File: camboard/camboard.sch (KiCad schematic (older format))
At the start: 36 parts

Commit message: Fixed camera connections
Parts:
- removed U?: STM32F746VGT6, symbol STM32F746VGT6
- added U?: STM32F746VGT6, symbol STM32F746VGT6
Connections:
- net labels added: DCMI_D0, DCMI_D1, DCMI_D2, DCMI_D3, DCMI_D4, DCMI_D5, DCMI_D6, DCMI_D7, DCMI_PWDN, WKUP
- wire segments 61 -> 82
- no-connect marks 7 -> 10
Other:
- moved on the sheet: J?
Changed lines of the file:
@@
 L PPTC102LFBN-RC J?
 U 1 1 59CC1D8B
-P 3200 2350
-F 0 "J?" H 3350 2850 50  0000 C CNN
-F 1 "PPTC102LFBN-RC" H 3400 1750 50  0000 C CNN
-F 2 "Pin_Headers:Pin_Header_Straight_2x10_Pitch2.54mm" H 1850 2200 50  0001 C CNN
-F 3 "" H 3500 2850 50  0001 C CNN
-	1    3200 2350
+P 4350 2400
+F 0 "J?" H 4500 2900 50  0000 C CNN
+F 1 "PPTC102LFBN-RC" H 4550 1800 50  0000 C CNN
+F 2 "Pin_Headers:Pin_Header_Straight_2x10_Pitch2.54mm" H 3000 2250 50  0001 C CNN
+F 3 "" H 4650 2900 50  0001 C CNN
+	1    4350 2400
 	1    0    0    -1
 $EndComp
 Text Label 8200 5325 1    60   ~ 0
 OSC25M
-Text Label 4000 2250 0    60   ~ 0
+Text Label 4150 2500 2    60   ~ 0
 OSC25M
-$Comp
-L STM32F746VGT6 U?
-U 1 1 59CAFAA7
-P 1125 2050
-F 0 "U?" H 1325 2300 60  0000 L CNN
-F 1 "STM32F746VGT6" H 1325 2200 60  0000 L CNN
-F 2 "" H 1125 2050 60  0001 C CNN
-F 3 "" H 1125 2050 60  0001 C CNN
-	1    1125 2050
-	1    0    0    -1
-$EndComp
-NoConn ~ 3000 2050
-NoConn ~ 3750 2050
 $Comp
 L +3V3 #PWR?
 U 1 1 59CC45D1
-P 3000 1950
-F 0 "#PWR?" H 3000 1800 50  0001 C CNN
-F 1 "+3V3" H 3000 2090 50  0000 C CNN
-F 2 "" H 3000 1950 50  0001 C CNN
-F 3 "" H 3000 1950 50  0001 C CNN
-	1    3000 1950
+P 4150 2000
+F 0 "#PWR?" H 4150 1850 50  0001 C CNN
+F 1 "+3V3" H 4150 2140 50  0000 C CNN
+F 2 "" H 4150 2000 50  0001 C CNN
+F 3 "" H 4150 2000 50  0001 C CNN
+	1    4150 2000
 	1    0    0    -1
 $EndComp
@@
 L GND #PWR?
 U 1 1 59CC4735
-P 3900 1950
-F 0 "#PWR?" H 3900 1700 50  0001 C CNN
-F 1 "GND" H 3900 1800 50  0000 C CNN
-F 2 "" H 3900 1950 50  0001 C CNN
-F 3 "" H 3900 1950 50  0001 C CNN
-	1    3900 1950
+P 4150 2900
+F 0 "#PWR?" H 4150 2650 50  0001 C CNN
+F 1 "GND" H 4150 2750 50  0000 C CNN
+F 2 "" H 4150 2900 50  0001 C CNN
+F 3 "" H 4150 2900 50  0001 C CNN
+	1    4150 2900
 	1    0    0    -1
 $EndComp
@@
 Text Label 1850 5975 0    60   ~ 0
 USB_5V
-Wire Wire Line
-	7700 5375 7375 5375
-Wire Wire Line
-	7375 5375 7375 5825
-Wire Wire Line
-	7675 5825 7700 5825
-Wire Wire Line
-	7700 5825 7700 5675
-Wire Wire Line
-	10000 5525 10450 5525
-Wire Wire Line
-	10000 5825 10450 5825
-Connection ~ 10225 5525
-Connection ~ 10225 5825
-Wire Wire Line
-	9700 5625 9700 5825
-Wire Wire Line
-	3550 6175 5225 6175
-Wire Wire Line
-	5225 6175 5225 6475
-Wire Wire Line
-	5225 6475 5150 6475
-Wire Wire Line
-	5150 6375 5150 6250
-Wire Wire Line
-	5150 6250 3550 6250
-Wire Wire Line
-	3550 6250 3550 6275
-Wire Wire Line
-	2825 4250 3625 4250
-Wire Wire Line
-	2900 4250 2900 3875
-Wire Wire Line
-	2825 4350 3625 4350
-Wire Wire Line
-	3050 4350 3050 3875
-Wire Wire Line
-	2825 4450 3625 4450
-Wire Wire Line
-	3200 4450 3200 3875
-Wire Wire Line
-	2825 4550 3625 4550
-Wire Wire Line
-	3350 4550 3350 3875
-Wire Wire Line
-	2825 4650 3625 4650
-Wire Wire Line
-	3500 4650 3500 3875
-Wire Wire Line
-	2825 4150 3625 4150
-Connection ~ 2900 4250
-Connection ~ 3050 4350
-Connection ~ 3200 4450
-Connection ~ 3350 4550
-Connection ~ 3500 4650
-Wire Wire Line
-	2900 3575 3500 3575
-Connection ~ 3050 3575
-Connection ~ 3200 3575
-Connection ~ 3350 3575
-Wire Wire Line
-	2725 2550 2850 2550
-Wire Wire Line
-	2850 2550 2850 2250
-Wire Wire Line
-	2850 2250 3000 2250
-Wire Wire Line
-	8200 5525 8200 5325
-Wire Wire Line
-	3000 2850 2725 2850
-Wire Wire Line
-	2725 2850 2725 2650
-Wire Wire Line
-	2725 2450 2800 2450
-Wire Wire Line
-	2800 2450 2800 3025
-Wire Wire Line
-	2800 3025 3750 3025
-Wire Wire Line
-	3750 3025 3750 2850
-Wire Wire Line
-	3750 1950 3900 1950
-Wire Wire Line
-	4000 2250 3750 2250
-Wire Wire Line
-	6275 1000 6375 1000
-Connection ~ 6325 1000
-Wire Wire Line
-	6975 1300 7450 1300
-Wire Wire Line
-	7450 1300 7450 1600
-Wire Wire Line
-	6975 1700 7450 1700
-Wire Wire Line
-	6975 1800 7450 1800
-Wire Wire Line
-	6975 1900 7450 1900
-Wire Wire Line
-	6975 2000 7450 2000
-Wire Wire Line
-	6975 2300 7025 2300
-Wire Wire Line
-	7025 2300 7025 2375
-Wire Wire Line
-	6975 2200 7200 2200
-Wire Wire Line
-	7200 2200 7200 2375
-Wire Wire Line
-	6975 1600 7375 1600
-Wire Wire Line
-	7375 1600 7375 2375
-Wire Wire Line
-	2075 7275 2950 7275
-Connection ~ 2850 7275
-Wire Wire Line
-	1975 6825 2075 6825
-Wire Wire Line
-	2075 6675 2075 6975
-Wire Wire Line
-	2075 6675 2150 6675
-Wire Wire Line
-	2150 6775 2075 6775
-Connection ~ 2075 6775
-Wire Wire Line
-	2075 6875 2150 6875
-Connection ~ 2075 6825
-Wire Wire Line
-	2075 6975 2150 6975
-Connection ~ 2075 6875
 $Comp
 L GND #PWR?
@@
 	1    0    0    -1
 $EndComp
-Connection ~ 2750 7275
 $Comp
 L LED D?
@@
 	1    0    0    -1
 $EndComp
-Wire Wire Line
-	5550 6650 5550 6775
-Wire Wire Line
-	5550 6775 3550 6775
-Wire Wire Line
-	5875 6650 5875 6875
-Wire Wire Line
-	5875 6875 3550 6875
 Text Notes 8825 6350 0    60   ~ 0
 Oscillators
@@
 Text Notes 2850 5325 0    60   ~ 0
 uSD Card
-Text Notes 2400 3250 0    60   ~ 0
+Text Notes 2250 3050 0    60   ~ 0
 Camera DCMI
 Text Notes 6450 3075 0    60   ~ 0
@@
 Text Notes 1900 1575 0    60   ~ 0
 Power
+$Comp
+L STM32F746VGT6 U?
+U 1 1 59CD63AE
+P 1650 2000
+F 0 "U?" H 1850 2250 60  0000 L CNN
+F 1 "STM32F746VGT6" H 1850 2150 60  0000 L CNN
+F 2 "" H 1650 2000 60  0001 C CNN
+F 3 "" H 1650 2000 60  0001 C CNN
+	1    1650 2000
+	1    0    0    -1
+$EndComp
+NoConn ~ 3350 2300
+NoConn ~ 3350 2400
+Text Label 1650 2000 2    60   ~ 0
+DCMI_D0
+Text Label 1650 2100 2    60   ~ 0
+DCMI_D1
+Text Label 1650 2200 2    60   ~ 0
+DCMI_D2
+Text Label 1650 2300 2    60   ~ 0
+DCMI_D3
+Text Label 1650 2400 2    60   ~ 0
+DCMI_D4
+Text Label 1650 2500 2    60   ~ 0
+DCMI_D5
+Text Label 1650 2700 2    60   ~ 0
+DCMI_D6
+Text Label 1650 2800 2    60   ~ 0
+DCMI_D7
+NoConn ~ 1650 2600
+Wire Wire Line
+	7700 5375 7375 5375
+Wire Wire Line
+	7375 5375 7375 5825
+Wire Wire Line
+	7675 5825 7700 5825
+Wire Wire Line
+	7700 5825 7700 5675
+Wire Wire Line
+	10000 5525 10450 5525
+Wire Wire Line
+	10000 5825 10450 5825
+Connection ~ 10225 5525
+Connection ~ 10225 5825
+Wire Wire Line
+	9700 5625 9700 5825
+Wire Wire Line
+	3550 6175 5225 6175
+Wire Wire Line
+	5225 6175 5225 6475
+Wire Wire Line
+	5225 6475 5150 6475
+Wire Wire Line
+	5150 6375 5150 6250
+Wire Wire Line
+	5150 6250 3550 6250
+Wire Wire Line
+	3550 6250 3550 6275
+Wire Wire Line
+	2825 4250 3625 4250
+Wire Wire Line
+	2900 4250 2900 3875
+Wire Wire Line
+	2825 4350 3625 4350
+Wire Wire Line
+	3050 4350 3050 3875
+Wire Wire Line
+	2825 4450 3625 4450
+Wire Wire Line
+	3200 4450 3200 3875
+Wire Wire Line
+	2825 4550 3625 4550
+Wire Wire Line
+	3350 4550 3350 3875
+Wire Wire Line
+	2825 4650 3625 4650
+Wire Wire Line
+	3500 4650 3500 3875
+Wire Wire Line
+	2825 4150 3625 4150
+Connection ~ 2900 4250
+Connection ~ 3050 4350
+Connection ~ 3200 4450
+Connection ~ 3350 4550
+Connection ~ 3500 4650
+Wire Wire Line
+	2900 3575 3500 3575
+Connection ~ 3050 3575
+Connection ~ 3200 3575
+Connection ~ 3350 3575
+Wire Wire Line
+	8200 5525 8200 5325
+Wire Wire Line
+	6275 1000 6375 1000
+Connection ~ 6325 1000
+Wire Wire Line
+	6975 1300 7450 1300
+Wire Wire Line
+	7450 1300 7450 1600
+Wire Wire Line
+	6975 1700 7450 1700
+Wire Wire Line
+	6975 1800 7450 1800
+Wire Wire Line
+	6975 1900 7450 1900
+Wire Wire Line
+	6975 2000 7450 2000
+Wire Wire Line
+	6975 2300 7025 2300
+Wire Wire Line
+	7025 2300 7025 2375
+Wire Wire Line
+	6975 2200 7200 2200
+Wire Wire Line
+	7200 2200 7200 2375
+Wire Wire Line
+	6975 1600 7375 1600
+Wire Wire Line
+	7375 1600 7375 2375
+Wire Wire Line
+	2075 7275 2950 7275
+Connection ~ 2850 7275
+Wire Wire Line
+	2075 6825 1975 6825
+Wire Wire Line
+	2075 6675 2075 6975
+Wire Wire Line
+	2075 6675 2150 6675
+Wire Wire Line
+	2150 6775 2075 6775
+Connection ~ 2075 6775
+Wire Wire Line
+	2075 6875 2150 6875
+Connection ~ 2075 6825
+Wire Wire Line
+	2075 6975 2150 6975
+Connection ~ 2075 6875
+Connection ~ 2750 7275
+Wire Wire Line
+	5550 6650 5550 6775
+Wire Wire Line
+	5550 6775 3550 6775
+Wire Wire Line
+	5875 6650 5875 6875
+Wire Wire Line
+	5875 6875 3550 6875
+Wire Wire Line
+	1650 2000 1200 2000
+Wire Wire Line
+	1650 2100 1200 2100
+Wire Wire Line
+	1650 2200 1200 2200
+Wire Wire Line
+	1650 2300 1200 2300
+Wire Wire Line
+	1650 2400 1200 2400
+Wire Wire Line
+	1650 2500 1200 2500
+Wire Wire Line
+	1650 2700 1200 2700
+Wire Wire Line
+	1650 2800 1200 2800
+Wire Wire Line
+	3350 2100 4150 2100
+Wire Wire Line
+	4150 2200 3350 2200
+Wire Wire Line
+	3350 2500 3500 2500
+Wire Wire Line
+	3500 2500 3500 2300
+Wire Wire Line
+	3500 2300 4150 2300
+Wire Wire Line
+	3350 2600 3550 2600
+Wire Wire Line
+	3550 2600 3550 2400
+Wire Wire Line
+	3550 2400 4150 2400
+Wire Wire Line
+	4150 2500 3800 2500
+Wire Wire Line
+	3350 2700 3575 2700
+Wire Wire Line
+	3575 2700 3575 2600
+Wire Wire Line
+	3575 2600 4150 2600
+Text Label 4900 2000 0    60   ~ 0
+DCMI_D0
+Text Label 4900 2100 0    60   ~ 0
+DCMI_D1
+Text Label 4900 2200 0    60   ~ 0
+DCMI_D2
+Text Label 4900 2300 0    60   ~ 0
+DCMI_D3
+Text Label 4900 2400 0    60   ~ 0
+DCMI_D4
+Text Label 4900 2500 0    60   ~ 0
+DCMI_D5
+Text Label 4900 2600 0    60   ~ 0
+DCMI_D6
+Text Label 4900 2700 0    60   ~ 0
+DCMI_D7
+Wire Wire Line
+	4900 2000 5350 2000
+Wire Wire Line
+	4900 2100 5350 2100
+Wire Wire Line
+	4900 2200 5350 2200
+Wire Wire Line
+	4900 2300 5350 2300
+Wire Wire Line
+	4900 2400 5350 2400
+Wire Wire Line
+	4900 2500 5350 2500
+Wire Wire Line
+	4900 2600 5350 2600
+Wire Wire Line
+	4900 2700 5350 2700
+Wire Bus Line
+	1200 2000 1200 3100
+Wire Bus Line
+	1200 3100 5350 3100
+Wire Bus Line
+	5350 3100 5350 2000
+NoConn ~ 4900 2800
+NoConn ~ 4900 2900
+Text Label 9375 825  2    60   ~ 0
+WKUP
+Wire Wire Line
+	9375 825  9075 825
+Text Label 4150 2700 2    60   ~ 0
+WKUP
+Wire Wire Line
+	4150 2700 3900 2700
+Wire Wire Line
+	9375 925  9075 925
+Text Label 9375 925  2    60   ~ 0
+DCMI_PWDN
+Text Label 4150 2800 2    60   ~ 0
+DCMI_PWDN
+Wire Wire Line
+	4150 2800 3650 2800
 $EndSCHEMATC

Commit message: Added bypass caps
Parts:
- added C1: 4.7uF, symbol C
- added C2 (x7): 100nF, symbol C
- added C3 (x2): 1uF, symbol C
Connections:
- wire segments 82 -> 91
- no-connect marks 10 -> 11
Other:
- moved on the sheet: C?, D?, J?, R?, U?, U?A, U?E, U?G

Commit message: Fixed some issues
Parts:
- added C15, C16: 2.2uF, symbol C
- added R15: 10k, symbol R
- added unit 2 of SW1
- gave numbers to parts that had none: 30
- renumbered C2 to C10, C2 to C11, C2 to C12, C2 to C13, C2 to C14, C3 to C2, C2 to C8, C2 to C9
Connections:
- wire segments 91 -> 96
- no-connect marks 11 -> 16
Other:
- note added: "RX indicator"
- note added: "TX indicator"

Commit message: added USB micro
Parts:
- removed J1: USB_B, symbol USB_B
- added J1: USB_microB_2040002-1, symbol USB_microB_2040002-1
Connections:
- wire segments 96 -> 102
- no-connect marks 16 -> 21
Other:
- moved on the sheet: C4, D1, D2, R1, R2, U1G, U3

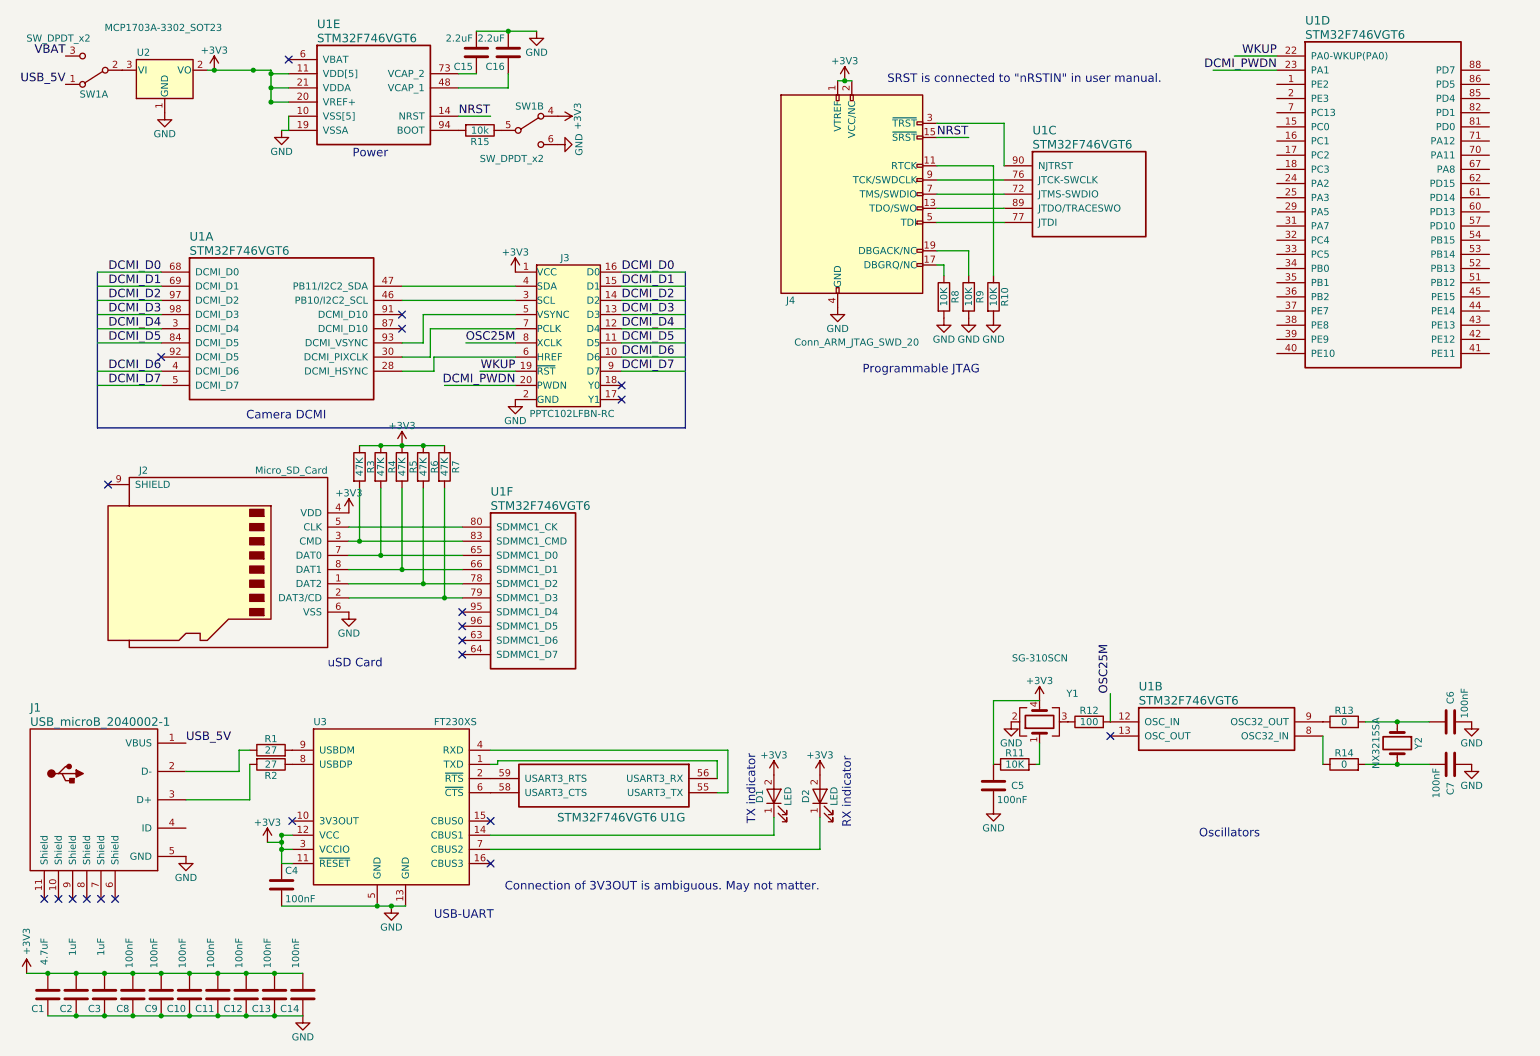
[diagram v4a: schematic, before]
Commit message: modified resistor values, etc.
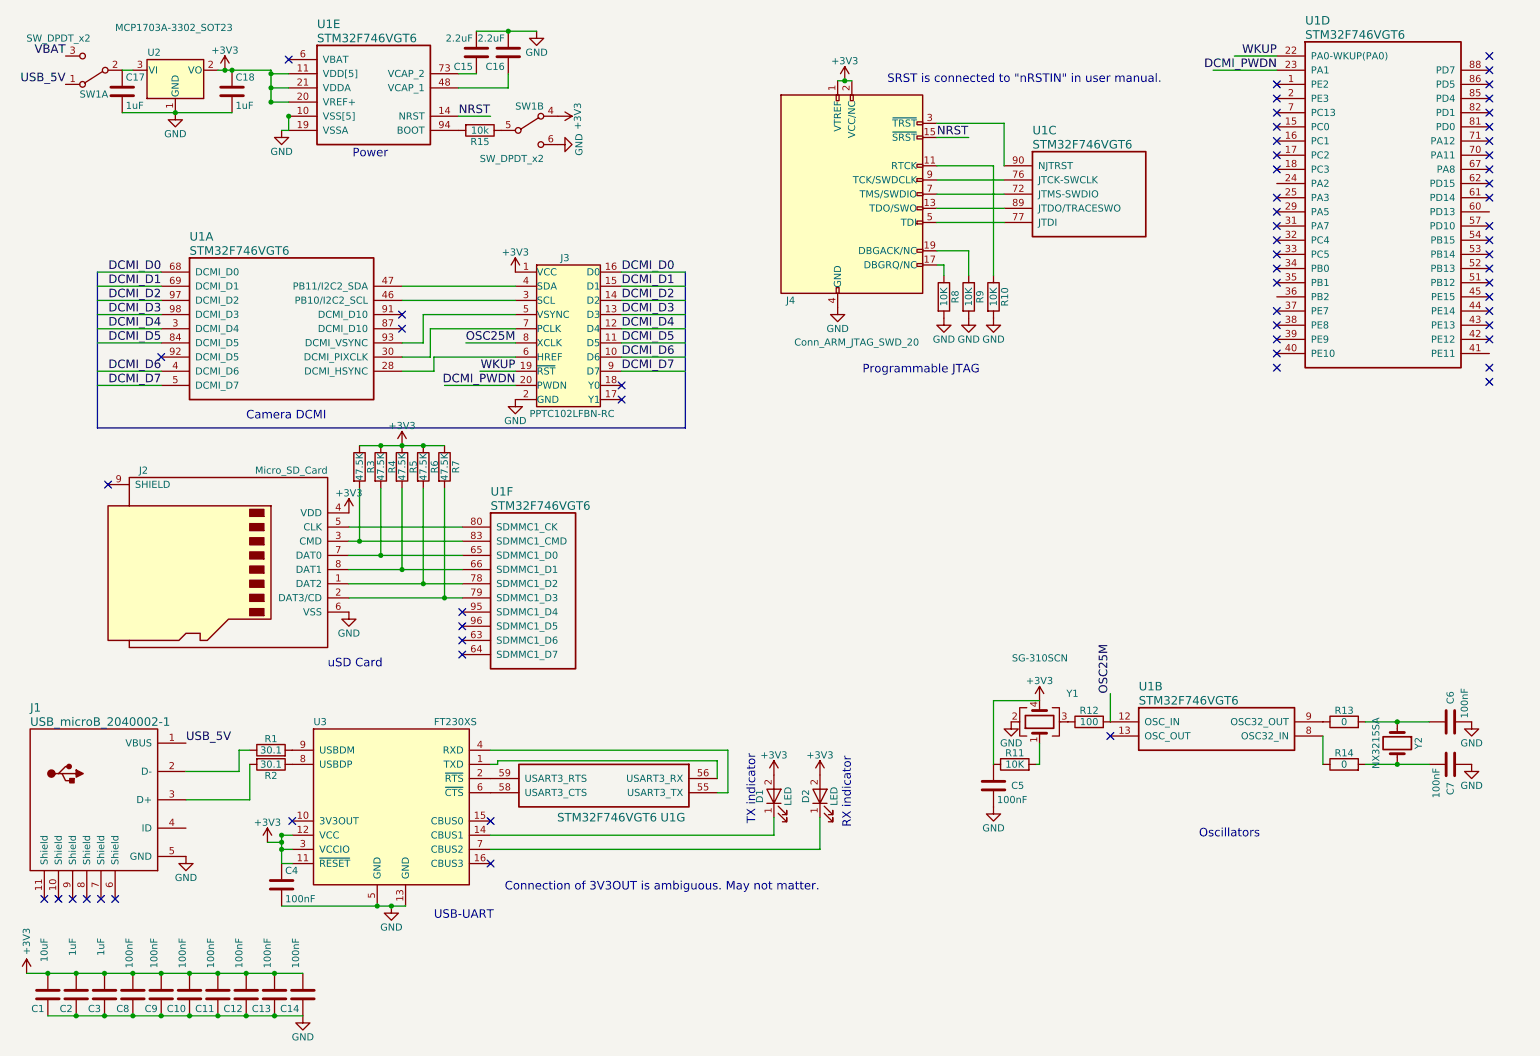
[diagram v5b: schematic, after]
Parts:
- added C17, C18: 1uF, symbol C
- C1: value 4.7uF -> 10uF
- R1, R2: value 27 -> 30.1
- R3, R4, R5, R6, R7: value 47K -> 47.5K
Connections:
- wire segments 102 -> 104
- no-connect marks 21 -> 62
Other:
- moved on the sheet: U2
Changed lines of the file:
@@
 L MCP1703A-3302_SOT23 U2
 U 1 1 59CBD041
-P 1525 925
-F 0 "U2" H 1375 1050 50  0000 C CNN
-F 1 "MCP1703A-3302_SOT23" H 1100 1225 50  0000 L CNN
-F 2 "TO_SOT_Packages_SMD:SOT-23" H 1525 1125 50  0001 C CNN
-F 3 "" H 1525 875 50  0001 C CNN
-	1    1525 925
+P 1600 925
+F 0 "U2" H 1450 1050 50  0000 C CNN
+F 1 "MCP1703A-3302_SOT23" H 1175 1225 50  0000 L CNN
+F 2 "TO_SOT_Packages_SMD:SOT-23" H 1600 1125 50  0001 C CNN
+F 3 "" H 1600 875 50  0001 C CNN
+	1    1600 925
 	1    0    0    -1
 $EndComp
@@
 L GND #PWR06
 U 1 1 59CBD66A
-P 1525 1225
-F 0 "#PWR06" H 1525 975 50  0001 C CNN
-F 1 "GND" H 1525 1075 50  0000 C CNN
-F 2 "" H 1525 1225 50  0001 C CNN
-F 3 "" H 1525 1225 50  0001 C CNN
-	1    1525 1225
+P 1600 1225
+F 0 "#PWR06" H 1600 975 50  0001 C CNN
+F 1 "GND" H 1600 1075 50  0000 C CNN
+F 2 "" H 1600 1225 50  0001 C CNN
+F 3 "" H 1600 1225 50  0001 C CNN
+	1    1600 1225
 	1    0    0    -1
 $EndComp
@@
 L +3V3 #PWR07
 U 1 1 59CBD92A
-P 1875 925
-F 0 "#PWR07" H 1875 775 50  0001 C CNN
-F 1 "+3V3" H 1875 1065 50  0000 C CNN
-F 2 "" H 1875 925 50  0001 C CNN
-F 3 "" H 1875 925 50  0001 C CNN
-	1    1875 925
+P 1950 925
+F 0 "#PWR07" H 1950 775 50  0001 C CNN
+F 1 "+3V3" H 1950 1065 50  0000 C CNN
+F 2 "" H 1950 925 50  0001 C CNN
+F 3 "" H 1950 925 50  0001 C CNN
+	1    1950 925
 	1    0    0    -1
 $EndComp
@@
 P 2900 3725
 F 0 "R3" V 2980 3725 50  0000 C CNN
-F 1 "47K" V 2900 3725 50  0000 C CNN
+F 1 "47.5K" V 2900 3725 50  0000 C CNN
 F 2 "" V 2830 3725 50  0001 C CNN
 F 3 "" H 2900 3725 50  0001 C CNN
@@
 P 3050 3725
 F 0 "R4" V 3130 3725 50  0000 C CNN
-F 1 "47K" V 3050 3725 50  0000 C CNN
+F 1 "47.5K" V 3050 3725 50  0000 C CNN
 F 2 "" V 2980 3725 50  0001 C CNN
 F 3 "" H 3050 3725 50  0001 C CNN
@@
 P 3200 3725
 F 0 "R5" V 3280 3725 50  0000 C CNN
-F 1 "47K" V 3200 3725 50  0000 C CNN
+F 1 "47.5K" V 3200 3725 50  0000 C CNN
 F 2 "" V 3130 3725 50  0001 C CNN
 F 3 "" H 3200 3725 50  0001 C CNN
@@
 P 3350 3725
 F 0 "R6" V 3430 3725 50  0000 C CNN
-F 1 "47K" V 3350 3725 50  0000 C CNN
+F 1 "47.5K" V 3350 3725 50  0000 C CNN
 F 2 "" V 3280 3725 50  0001 C CNN
 F 3 "" H 3350 3725 50  0001 C CNN
@@
 P 3500 3725
 F 0 "R7" V 3580 3725 50  0000 C CNN
-F 1 "47K" V 3500 3725 50  0000 C CNN
+F 1 "47.5K" V 3500 3725 50  0000 C CNN
 F 2 "" V 3430 3725 50  0001 C CNN
 F 3 "" H 3500 3725 50  0001 C CNN
@@
 P 2275 5825
 F 0 "R2" V 2355 5825 50  0000 C CNN
-F 1 "27" V 2275 5825 50  0000 C CNN
+F 1 "30.1" V 2275 5825 50  0000 C CNN
 F 2 "" V 2205 5825 50  0001 C CNN
 F 3 "" H 2275 5825 50  0001 C CNN
@@
 P 2275 5725
 F 0 "R1" V 2355 5725 50  0000 C CNN
-F 1 "27" V 2275 5725 50  0000 C CNN
+F 1 "30.1" V 2275 5725 50  0000 C CNN
 F 2 "" V 2205 5725 50  0001 C CNN
 F 3 "" H 2275 5725 50  0001 C CNN
@@
 P 700 7450
 F 0 "C1" H 725 7550 50  0000 L CNN
-F 1 "4.7uF" V 725 7050 50  0000 L CNN
+F 1 "10uF" V 725 7050 50  0000 L CNN
 F 2 "" H 738 7300 50  0001 C CNN
 F 3 "" H 700 7450 50  0001 C CNN
@@
 	4000 3150 3500 3150
 Wire Wire Line
-	1825 925  2275 925
-Connection ~ 1875 925
-Wire Wire Line
 	2400 1250 2400 1350
 Wire Wire Line
 	2400 1350 2350 1350
-Connection ~ 2150 925
 Wire Wire Line
 	2275 925  2275 1150
@@
 Wire Wire Line
 	5500 5725 5500 6025
+$Comp
+L C C18
+U 1 1 59CEC20B
+P 2000 1075
+F 0 "C18" H 2025 1175 50  0000 L CNN
+F 1 "1uF" H 2025 975 50  0000 L CNN
+F 2 "" H 2038 925 50  0001 C CNN
+F 3 "" H 2000 1075 50  0001 C CNN
+	1    2000 1075
+	1    0    0    -1
+$EndComp
+Wire Wire Line
+	1225 1225 2000 1225
+$Comp
+L C C17
+U 1 1 59CEC490
+P 1225 1075
+F 0 "C17" H 1250 1175 50  0000 L CNN
+F 1 "1uF" H 1250 975 50  0000 L CNN
+F 2 "" H 1263 925 50  0001 C CNN
+F 3 "" H 1225 1075 50  0001 C CNN
+	1    1225 1075
+	1    0    0    -1
+$EndComp
+NoConn ~ 9375 1025
+NoConn ~ 9375 1125
+NoConn ~ 9375 1225
+NoConn ~ 9375 1325
+NoConn ~ 9375 1425
+NoConn ~ 9375 1525
+NoConn ~ 9375 1625
+NoConn ~ 9375 1825
+NoConn ~ 9375 1925
+NoConn ~ 9375 2025
+NoConn ~ 9375 2125
+NoConn ~ 9375 2225
+NoConn ~ 9375 2325
+NoConn ~ 9375 2425
+NoConn ~ 9375 2625
+NoConn ~ 9375 2725
+NoConn ~ 9375 2825
+NoConn ~ 9375 2925
+NoConn ~ 9375 3025
+NoConn ~ 10875 825
+NoConn ~ 10875 925
+NoConn ~ 10875 1025
+NoConn ~ 10875 1125
+NoConn ~ 10875 1225
+NoConn ~ 10875 1325
+NoConn ~ 10875 1425
+NoConn ~ 10875 1525
+NoConn ~ 10875 1625
+NoConn ~ 10875 1725
+NoConn ~ 10875 1825
+NoConn ~ 10875 2025
+NoConn ~ 10875 2125
+NoConn ~ 10875 2225
+NoConn ~ 10875 2325
+NoConn ~ 10875 2425
+NoConn ~ 10875 2525
+NoConn ~ 10875 2625
+NoConn ~ 10875 2725
+NoConn ~ 10875 2825
+NoConn ~ 10875 3025
+NoConn ~ 10875 3125
+Connection ~ 2400 1250
+Connection ~ 1600 1225
+Wire Wire Line
+	1900 925  2275 925
+Connection ~ 1950 925
+Connection ~ 2000 925
+Wire Wire Line
+	1300 925  1225 925
 $EndSCHEMATC
